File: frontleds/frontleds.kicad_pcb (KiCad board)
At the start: 2 copper layers, 9.2 x 9.9 mm, 2 parts, among them J3 Conn_02x10_Odd_Even

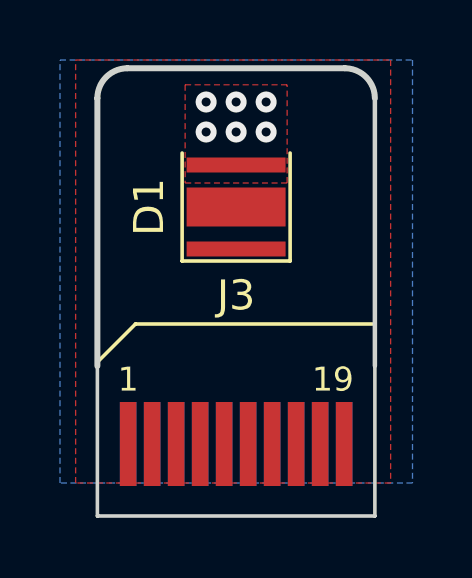
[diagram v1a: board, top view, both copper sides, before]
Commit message: bro how does this work (fix led symbol footprint and model)
idk why frontleds can use drylettuce symbols but not footprints/3d models liek whaaaaa
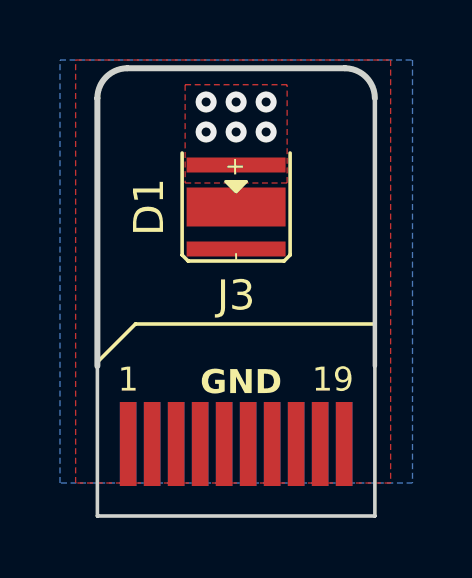
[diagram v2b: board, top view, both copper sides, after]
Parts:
- D1: value LED_Pad -> LED_CREE; footprint LED_SMD:LED_Cree-XP-GWT -> Dry_Lettuce_LED:LED_Cree-XPGBWT
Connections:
- D1 pad 1: GND -> /PWR
- D1 pad 2: /PWR -> GND
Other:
- board text added: "GND"
- board text added: "PWR"
